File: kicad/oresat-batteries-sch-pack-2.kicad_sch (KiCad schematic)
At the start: 79 parts, among them Q24 PM45VEN, Q25 PM45VEN, Q26 PM45VEN, Q27 PM45VEN, Q30 Q-VISHAY-MOSFET-PCH-POWERPAK-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, Q31 Q-VISHAY-MOSFET-PCH-POWERPAK-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, Q32 NTR4101, Q33 NTR4101, Q34 Q-VISHAY-MOSFET-PCH-POWERPAK-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, Q35 Q-VISHAY-MOSFET-PCH-POWERPAK-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, Q36 Q-VISHAY-MOSFET-PCH-POWERPAK-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, Q37 Q-VISHAY-MOSFET-PCH-POWERPAK-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, U13 S-8209AXXT, U14 S-8209AXXT, U15 LTC4412, U16 LTC4412, U17 MAX17205G

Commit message: Updating KiCAD import of EAGLE battery card v3.0 and calling it v3.1 because the gerber files will definitely be different and we'll probably implement a few small changes. Reimports, renames, and fixes .gitignore file. Oh and makes the worksheets pretty.
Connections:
- net DCHG-STAT-OC-PK2: now also Q31.4 (G), U15.5 (GATE)
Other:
- note removed: "1.0"
- note removed: "OreSat battery Card - Battery Pack 2"
- title: (none) -> OreSat Battery Card - Pack 2 (Top)
- moved on the sheet: B3, B4, C26, C27, C28, C29, C30, C31, C32, C33, C34, C35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

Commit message: Kicad import try #3. Now with DXFs from custom EAGLE layers. Schematic worksheets and names updated.
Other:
- title: OreSat Battery Card - Pack 2 (Top) -> OreSat Battery Card

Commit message: Move main connector to kicad libraries; start updating text size.
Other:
- title: OreSat Battery Card -> OreSat Battery Card - Pack 2 (Top)
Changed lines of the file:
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@@
   (paper "B")
   (title_block
-    (title "OreSat Battery Card")
+    (title "OreSat Battery Card - Pack 2 (Top)")
     (date "2023-12-02")
     (rev "3.1")

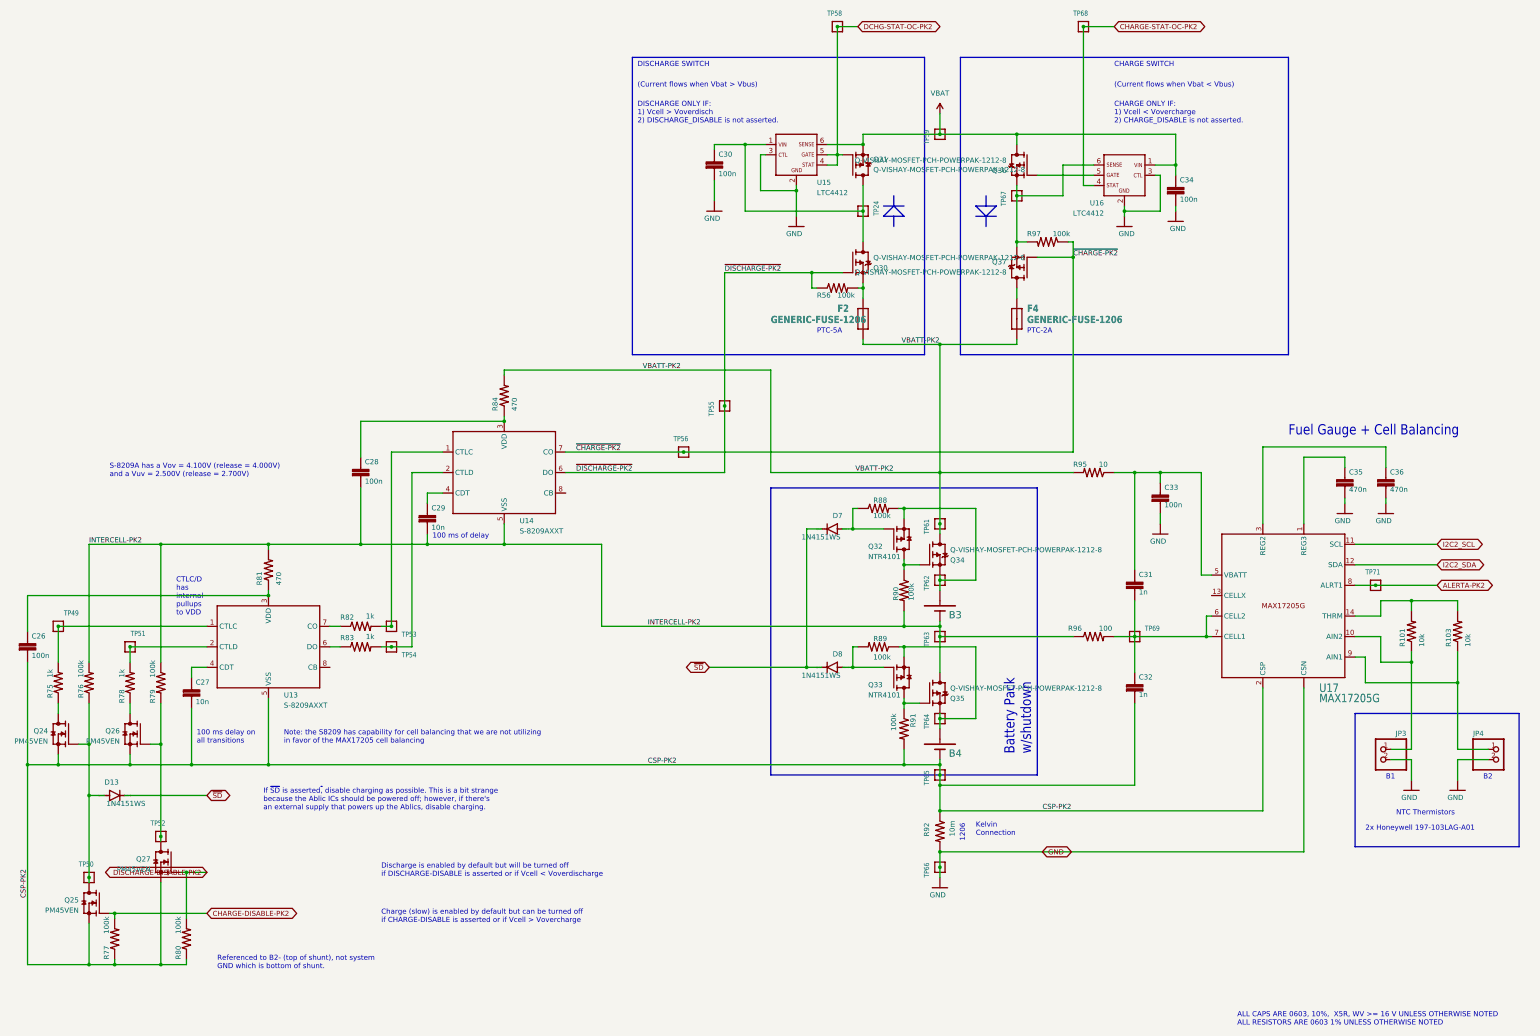
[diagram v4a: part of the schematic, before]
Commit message: Updated ground planes, battery foot prints, zones needs more work.
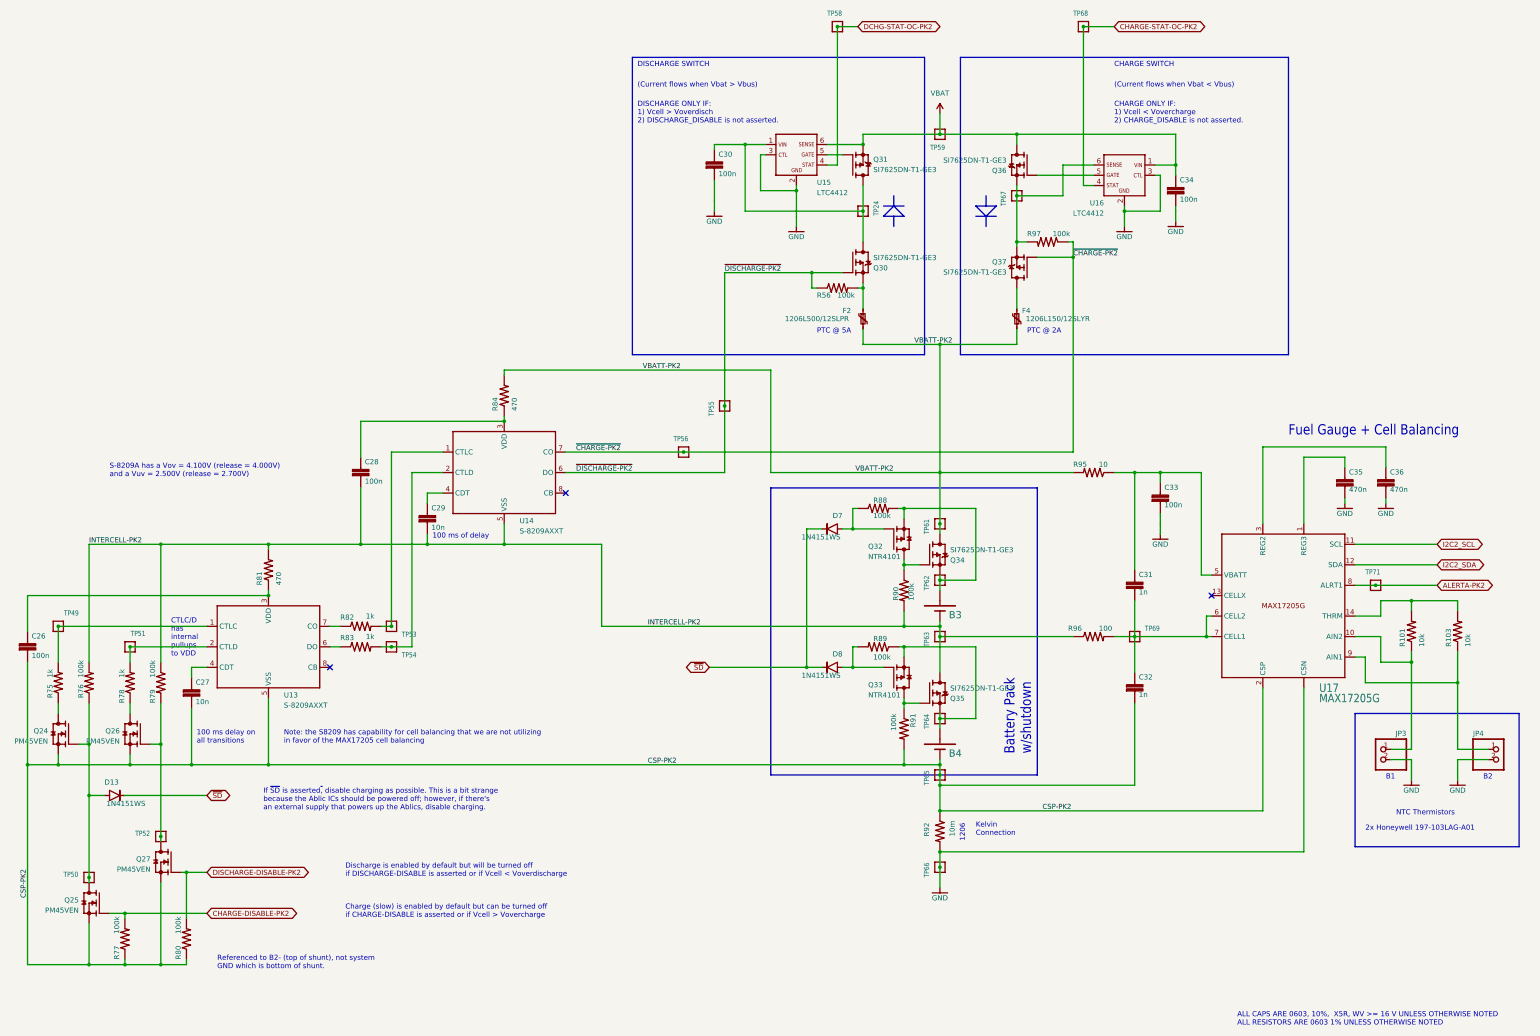
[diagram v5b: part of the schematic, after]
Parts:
- D13, D7, D8: footprint oresat-batteries:SOD323-R -> Diode_SMD:D_SOD-323; symbol oresat-batteries-eagle-import:DIODE-SOD323-R -> oresat-diodes:1N4151WS-HE3; DIS Digi-Key -> (none); DPN 112-1N4151WS-E3-08CT-ND -> (none); MFR Vishay -> (none); MPN 1N4151WS-E3-08 -> (none)
- F2: value GENERIC-FUSE-1206 -> 1206L500/12SLPR; footprint oresat-batteries:1206-C -> oresat-passives:1206-C; symbol oresat-batteries-eagle-import:GENERIC-FUSE-1206 -> Device:Polyfuse_Small; DIS Digi-Key -> (none); DPN F9966CT-ND -> (none); MFR LittleFuse -> (none); MPN NANOSMD350LR-C-2 -> (none)
- F4: value GENERIC-FUSE-1206 -> 1206L150/12SLYR; footprint oresat-batteries:1206-C -> oresat-passives:1206-C; symbol oresat-batteries-eagle-import:GENERIC-FUSE-1206 -> Device:Polyfuse_Small; DIS Digi-Key -> (none); DPN F9966CT-ND -> (none); MFR LittleFuse -> (none); MPN NANOSMD350LR-C-2 -> (none)
- Q30, Q31, Q34, Q35, Q36, Q37: value Q-VISHAY-MOSFET-PCH-POWERPAK-1212-8 -> SI7625DN-T1-GE3
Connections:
- net CSP-PK2: now also B4.2 (NEG); no longer B4.NEG-T (NEG)
- net DCHG-STAT-OC-PK2: no longer Q31.4 (G), U15.5 (GATE)
- net INTERCELL-PK2: now also B3.2 (NEG); no longer B3.NEG-T (NEG)
- net ~{SD}: now also D13.1, D7.1, D8.1; no longer D13.C, D7.C, D8.C
- net at Q24.1 (G), Q25.3 (D), R76.1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: now also D13.2; no longer D13.A
- net at Q32.2 (S), Q34.1 (S), Q34.2 (S)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: now also B3.1 (POS); no longer B3.POS-T (POS)
- net at Q33.2 (S), Q35.1 (S), Q35.2 (S)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: now also B4.1 (POS); no longer B4.POS-T (POS)
- net at Q32.1 (G), R88.1: now also D7.2; no longer D7.A
- net at Q33.1 (G), R89.2: now also D8.2; no longer D8.A
- new net: Q31.4 (G), U15.5 (GATE)
- no-connect marks 0 -> 3
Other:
- note added: "PTC @ 2A"
- note added: "PTC @ 5A"
- note removed: "PTC-2A"
- note removed: "PTC-5A"
- moved on the sheet: R77

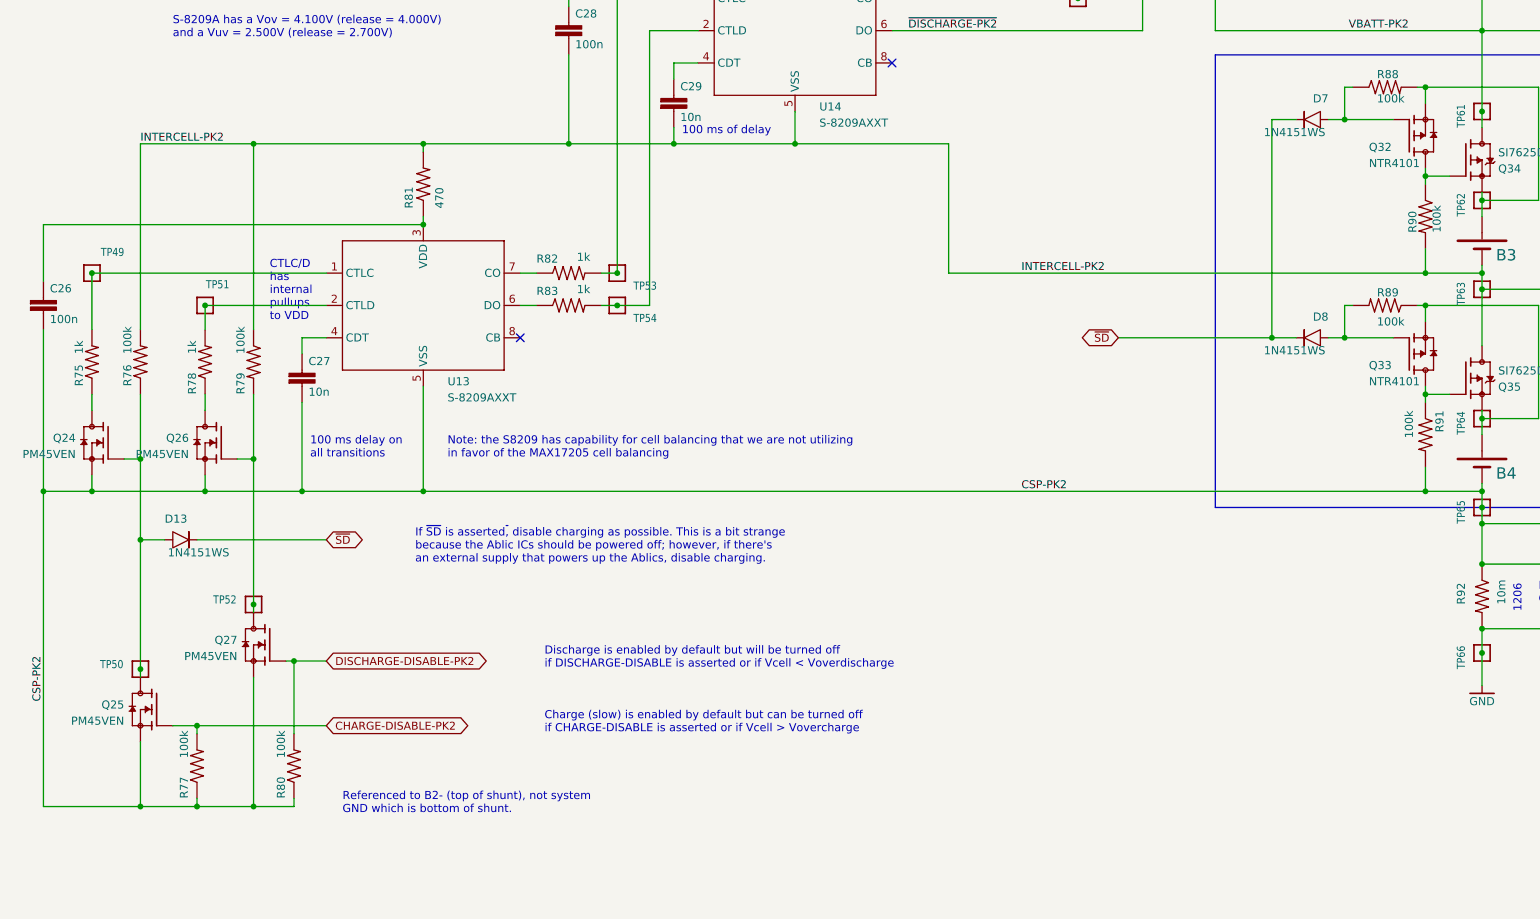
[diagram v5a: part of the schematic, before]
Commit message: better schematic layout (no netlist changes) on battery packs, and updated DRUs and fixed some minor DRU issues.
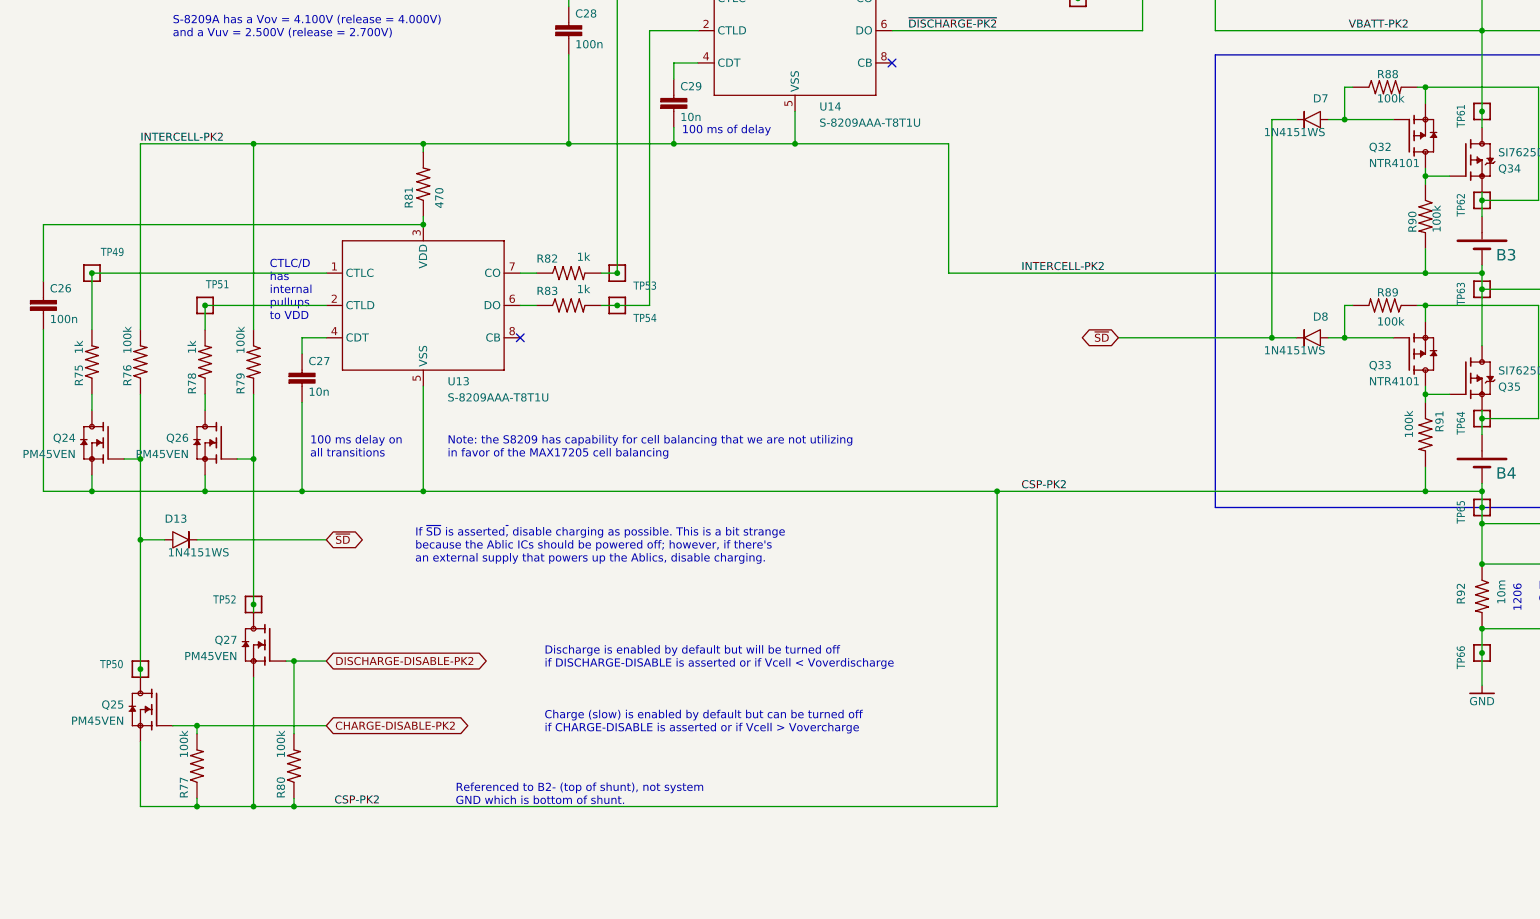
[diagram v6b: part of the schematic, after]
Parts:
- U13, U14: value S-8209AXXT -> S-8209AAA-T8T1U
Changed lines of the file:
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@@
   (junction (at 73.66 200.66) (diameter 0) (color 0 0 0 0)
   )
+  (junction (at 72.39 250.19) (diameter 0) (color 0 0 0 0)
+  )
   (junction (at 317.5 52.07) (diameter 0) (color 0 0 0 0)
   )
@@
   (junction (at 259.08 226.06) (diameter 0) (color 0 0 0 0)
   )
-  (junction (at 48.26 250.19) (diameter 0) (color 0 0 0 0)
+  (junction (at 182.88 200.66) (diameter 0) (color 0 0 0 0)
   )
   (junction (at 48.26 195.58) (diameter 0) (color 0 0 0 0)
@@
   (junction (at 375.92 160.02) (diameter 0) (color 0 0 0 0)
   )
-  (junction (at 33.02 200.66) (diameter 0) (color 0 0 0 0)
-  )
   (junction (at 40.64 166.37) (diameter 0) (color 0 0 0 0)
   )
@@
     (stroke (width 0.508) (type solid))
   )
+  (wire (pts (xy 72.39 250.19) (xy 182.88 250.19))
+    (stroke (width 0.1524) (type solid))
+  )
   (wire (pts (xy 214.63 49.53) (xy 214.63 58.42))
     (stroke (width 0.1524) (type solid))
@@
     (stroke (width 0.1524) (type solid))
   )
-  (wire (pts (xy 33.02 250.19) (xy 48.26 250.19))
-    (stroke (width 0.1524) (type solid))
-  )
   (polyline (pts (xy 270.51 62.23) (xy 273.05 62.23))
     (stroke (width 0.1524) (type solid))
@@
     (stroke (width 0.1524) (type solid))
   )
+  (wire (pts (xy 182.88 250.19) (xy 182.88 200.66))
+    (stroke (width 0.1524) (type solid))
+  )
   (wire (pts (xy 217.17 128.27) (xy 217.17 102.87))
     (stroke (width 0.1524) (type solid))
@@
     (stroke (width 0.1524) (type solid))
   )
+  (wire (pts (xy 182.88 200.66) (xy 92.71 200.66))
+    (stroke (width 0.1524) (type solid))
+  )
   (wire (pts (xy 33.02 167.64) (xy 33.02 158.75))
     (stroke (width 0.1524) (type solid))
@@
     (stroke (width 0.1524) (type solid))
   )
-  (wire (pts (xy 33.02 200.66) (xy 33.02 250.19))
-    (stroke (width 0.1524) (type solid))
-  )
   (wire (pts (xy 48.26 175.26) (xy 48.26 146.05))
     (stroke (width 0.1524) (type solid))
@@
     (stroke (width 0.1524) (type solid))
   )
-  (wire (pts (xy 250.19 200.66) (xy 92.71 200.66))
+  (wire (pts (xy 250.19 200.66) (xy 182.88 200.66))
     (stroke (width 0.1524) (type solid))
   )
@@
   )
   (text "Referenced to B2- (top of shunt), not system\nGND which is bottom of shunt."
-    (at 80.01 251.46 0)
+    (at 97.79 250.19 0)
     (effects (font (size 1.27 1.27)) (justify left bottom))
   )
@@
     (effects (font (size 1.2446 1.2446)) (justify left bottom))
   )
+  (label "CSP-PK2" (at 78.74 250.19 0) (fields_autoplaced)
+    (effects (font (size 1.2446 1.2446)) (justify left bottom))
+  )
   (label "~{DISCHARGE-PK2}" (at 168.91 128.27 0) (fields_autoplaced)
     (effects (font (size 1.2446 1.2446)) (justify left bottom))
@@
     (effects (font (size 1.2446 1.2446)) (justify left bottom))
   )
-  (label "CSP-PK2" (at 33.02 233.68 90) (fields_autoplaced)
-    (effects (font (size 1.2446 1.2446)) (justify left bottom))
-  )
   (label "CSP-PK2" (at 186.69 200.66 0) (fields_autoplaced)
     (effects (font (size 1.2446 1.2446)) (justify left bottom))
@@
       (effects (font (size 1.27 1.27)) (justify left bottom))
     )
-    (property "Value" "S-8209AXXT" (at 96.52 186.69 0)
+    (property "Value" "S-8209AAA-T8T1U" (at 96.52 186.69 0)
       (effects (font (size 1.27 1.27)) (justify left bottom))
     )
@@
       (effects (font (size 1.27 1.27)) hide)
     )
-    (property "Datasheet" "" (at 92.71 171.45 0)
+    (property "Datasheet" "https://www.ablic.com/en/doc/datasheet/battery_protection/S8209A_E.pdf" (at 92.71 171.45 0)
       (effects (font (size 1.27 1.27)) hide)
     )
@@
       (effects (font (size 1.27 1.27)) hide)
     )
-    (property "Datasheet" "" (at 304.8 54.61 0)
+    (property "Datasheet" "https://www.analog.com/media/en/technical-documentation/data-sheets/4412hvfs.pdf" (at 304.8 54.61 0)
       (effects (font (size 1.27 1.27)) hide)
     )
@@
       (effects (font (size 1.27 1.27)) hide)
     )
-    (property "Datasheet" "" (at 223.52 49.53 0)
+    (property "Datasheet" "https://www.analog.com/media/en/technical-documentation/data-sheets/4412hvfs.pdf" (at 223.52 49.53 0)
       (effects (font (size 1.27 1.27)) hide)
     )
@@
       (effects (font (size 1.27 1.27)) (justify left bottom))
     )
-    (property "Value" "S-8209AXXT" (at 154.94 143.51 0)
+    (property "Value" "S-8209AAA-T8T1U" (at 154.94 143.51 0)
       (effects (font (size 1.27 1.27)) (justify left bottom))
     )
@@
       (effects (font (size 1.27 1.27)) hide)
     )
-    (property "Datasheet" "" (at 151.13 128.27 0)
+    (property "Datasheet" "https://www.ablic.com/en/doc/datasheet/battery_protection/S8209A_E.pdf" (at 151.13 128.27 0)
       (effects (font (size 1.27 1.27)) hide)
     )
